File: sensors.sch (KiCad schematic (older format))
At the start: 18 parts

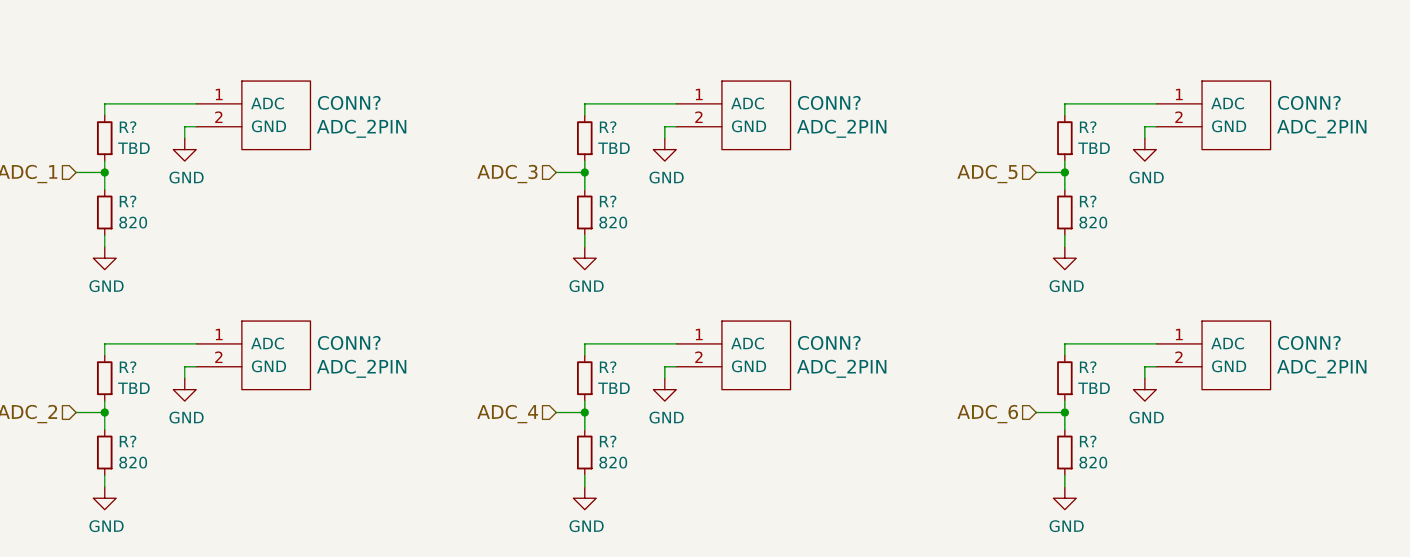
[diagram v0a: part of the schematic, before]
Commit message: Use 3pin connectors for ADC (with power pin)
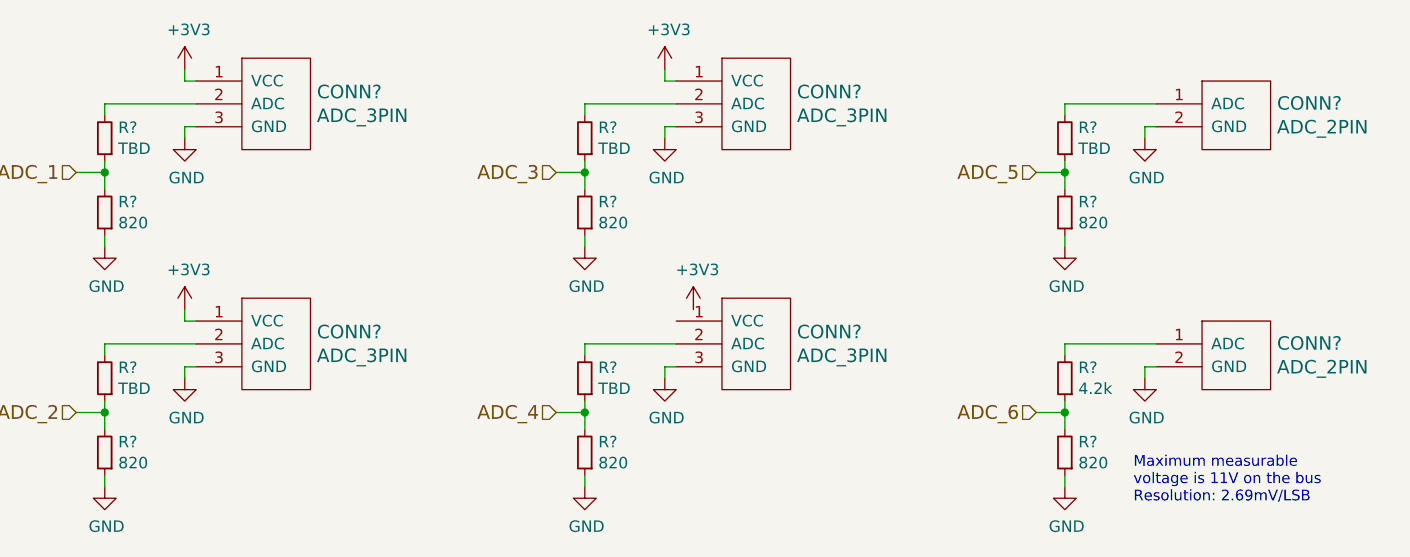
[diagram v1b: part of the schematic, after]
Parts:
- removed CONN? (x4): ADC_2PIN, symbol ADC_2PIN
- added CONN? (x4): ADC_3PIN, symbol ADC_3PIN
- R?: value TBD -> 4.2k
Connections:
- net GND: now also CONN?.3 (GND), CONN?.3 (GND), CONN?.3 (GND), CONN?.3 (GND)
- net at R?.2: now also CONN?.2 (ADC) (x4)
- new net +3V3: CONN?.1 (VCC), CONN?.1 (VCC), CONN?.1 (VCC)
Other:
- note added: "Maximum measurable \nvoltage is 11V on the bus\nResolution: 2.69mV/LSB"
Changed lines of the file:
@@
 Comment4 ""
 $EndDescr
-$Comp
-L ADC_2PIN CONN?
-U 1 1 569FF9E7
-P 2650 1750
-F 0 "CONN?" H 2828 2152 59  0000 L CNN
-F 1 "ADC_2PIN" H 2828 2048 59  0000 L CNN
-F 2 "" H 2650 1750 59  0000 C CNN
-F 3 "" H 2650 1750 59  0000 C CNN
-	1    2650 1750
-	1    0    0    -1
-$EndComp
 Text HLabel 1775 1650 0    60   Input ~ 0
 ADC_1
@@
 Wire Wire Line
 	1900 1975 1900 1925
-$Comp
-L ADC_2PIN CONN?
-U 1 1 56A00037
-P 2650 2800
-F 0 "CONN?" H 2828 3202 59  0000 L CNN
-F 1 "ADC_2PIN" H 2828 3098 59  0000 L CNN
-F 2 "" H 2650 2800 59  0000 C CNN
-F 3 "" H 2650 2800 59  0000 C CNN
-	1    2650 2800
-	1    0    0    -1
-$EndComp
 Text HLabel 1775 2700 0    60   Input ~ 0
 ADC_2
@@
 Wire Wire Line
 	1900 3025 1900 2975
-$Comp
-L ADC_2PIN CONN?
-U 1 1 56A00539
-P 4750 1750
-F 0 "CONN?" H 4928 2152 59  0000 L CNN
-F 1 "ADC_2PIN" H 4928 2048 59  0000 L CNN
-F 2 "" H 4750 1750 59  0000 C CNN
-F 3 "" H 4750 1750 59  0000 C CNN
-	1    4750 1750
-	1    0    0    -1
-$EndComp
 Text HLabel 3875 1650 0    60   Input ~ 0
 ADC_3
@@
 Wire Wire Line
 	4000 1975 4000 1925
-$Comp
-L ADC_2PIN CONN?
-U 1 1 56A00560
-P 4750 2800
-F 0 "CONN?" H 4928 3202 59  0000 L CNN
-F 1 "ADC_2PIN" H 4928 3098 59  0000 L CNN
-F 2 "" H 4750 2800 59  0000 C CNN
-F 3 "" H 4750 2800 59  0000 C CNN
-	1    4750 2800
-	1    0    0    -1
-$EndComp
 Text HLabel 3875 2700 0    60   Input ~ 0
 ADC_4
@@
 P 6100 2550
 F 0 "R?" H 6041 2504 50  0000 R CNN
-F 1 "TBD" H 6041 2596 50  0000 R CNN
+F 1 "4.2k" H 6041 2596 50  0000 R CNN
 F 2 "" H 6100 2550 50  0000 C CNN
 F 3 "" H 6100 2550 50  0000 C CNN
@@
 Wire Wire Line
 	6100 3025 6100 2975
+Text Notes 6400 3100 0    47   ~ 0
+Maximum measurable \nvoltage is 11V on the bus\nResolution: 2.69mV/LSB
+$Comp
+L ADC_3PIN CONN?
+U 1 1 56B05B1E
+P 2650 2800
+F 0 "CONN?" H 2828 3252 59  0000 L CNN
+F 1 "ADC_3PIN" H 2828 3148 59  0000 L CNN
+F 2 "" H 2650 2800 59  0000 C CNN
+F 3 "" H 2650 2800 59  0000 C CNN
+	1    2650 2800
+	1    0    0    -1
+$EndComp
+$Comp
+L ADC_3PIN CONN?
+U 1 1 56B05BE3
+P 2650 1750
+F 0 "CONN?" H 2828 2202 59  0000 L CNN
+F 1 "ADC_3PIN" H 2828 2098 59  0000 L CNN
+F 2 "" H 2650 1750 59  0000 C CNN
+F 3 "" H 2650 1750 59  0000 C CNN
+	1    2650 1750
+	1    0    0    -1
+$EndComp
+$Comp
+L +3V3 #PWR?
+U 1 1 56B05C70
+P 2250 2250
+F 0 "#PWR?" H 2250 2100 50  0001 C CNN
+F 1 "+3V3" H 2268 2424 50  0000 C CNN
+F 2 "" H 2250 2250 50  0000 C CNN
+F 3 "" H 2250 2250 50  0000 C CNN
+	1    2250 2250
+	1    0    0    -1
+$EndComp
+Wire Wire Line
+	2250 2250 2250 2300
+Wire Wire Line
+	2250 2300 2300 2300
+$Comp
+L +3V3 #PWR?
+U 1 1 56B05CFC
+P 2250 1200
+F 0 "#PWR?" H 2250 1050 50  0001 C CNN
+F 1 "+3V3" H 2268 1374 50  0000 C CNN
+F 2 "" H 2250 1200 50  0000 C CNN
+F 3 "" H 2250 1200 50  0000 C CNN
+	1    2250 1200
+	1    0    0    -1
+$EndComp
+Wire Wire Line
+	2250 1200 2250 1250
+Wire Wire Line
+	2250 1250 2300 1250
+$Comp
+L +3V3 #PWR?
+U 1 1 56B05E15
+P 4350 1200
+F 0 "#PWR?" H 4350 1050 50  0001 C CNN
+F 1 "+3V3" H 4368 1374 50  0000 C CNN
+F 2 "" H 4350 1200 50  0000 C CNN
+F 3 "" H 4350 1200 50  0000 C CNN
+	1    4350 1200
+	1    0    0    -1
+$EndComp
+$Comp
+L ADC_3PIN CONN?
+U 1 1 56B05E8E
+P 4750 1750
+F 0 "CONN?" H 4928 2202 59  0000 L CNN
+F 1 "ADC_3PIN" H 4928 2098 59  0000 L CNN
+F 2 "" H 4750 1750 59  0000 C CNN
+F 3 "" H 4750 1750 59  0000 C CNN
+	1    4750 1750
+	1    0    0    -1
+$EndComp
+Wire Wire Line
+	4350 1200 4350 1250
+Wire Wire Line
+	4350 1250 4400 1250
+$Comp
+L +3V3 #PWR?
+U 1 1 56B05F80
+P 4475 2250
+F 0 "#PWR?" H 4475 2100 50  0001 C CNN
+F 1 "+3V3" H 4493 2424 50  0000 C CNN
+F 2 "" H 4475 2250 50  0000 C CNN
+F 3 "" H 4475 2250 50  0000 C CNN
+	1    4475 2250
+	1    0    0    -1
+$EndComp
+$Comp
+L ADC_3PIN CONN?
+U 1 1 56B05FD2
+P 4750 2800
+F 0 "CONN?" H 4928 3252 59  0000 L CNN
+F 1 "ADC_3PIN" H 4928 3148 59  0000 L CNN
+F 2 "" H 4750 2800 59  0000 C CNN
+F 3 "" H 4750 2800 59  0000 C CNN
+	1    4750 2800
+	1    0    0    -1
+$EndComp
 $EndSCHEMATC

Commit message: Add RTC
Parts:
- added BT?: 3.6V, symbol Battery
- added C? (x2): 10p, symbol C_Small
- added C?: 220n, symbol C_Small
- added C?: 1u, symbol C_Small
- added U?: BQ32000, symbol BQ32000
- added X?: 32768Hz, symbol XTAL-SMD-4-PADS
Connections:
- net +3V3: now also C?.1, U?.8 (VCC)
- net GND: now also BT?.2, C?.2, C?.2, C?.2, C?.2, U?.4 (GND), X?.2 (case), X?.4 (case)
- new net: C?.1, U?.1 (OSCI), X?.3
- new net: C?.1, U?.2 (OSCO), X?.1
- new net: BT?.1, C?.1, U?.3 (V_BACK)
- new net I2C_SCL: U?.6 (SCL)
- new net I2C_SDA: U?.5 (SDA)
- no-connect marks 0 -> 1
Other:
- note added: "RTC\nI2C address: 0x68\nBattery: 1.4 to 3.6V"
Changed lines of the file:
@@
 Comment4 ""
 $EndDescr
-Text HLabel 1775 1650 0    60   Input ~ 0
+Text HLabel 1775 1650 0    47   Input ~ 0
 ADC_1
 $Comp
@@
 	1900 1350 2300 1350
 Wire Wire Line
-	1900 1600 1900 1725
+	1900 1600 1900 1650
+Wire Wire Line
+	1900 1650 1900 1725
 Wire Wire Line
 	1775 1650 1900 1650
@@
 Wire Wire Line
 	1900 1975 1900 1925
-Text HLabel 1775 2700 0    60   Input ~ 0
+Text HLabel 1775 2700 0    47   Input ~ 0
 ADC_2
 $Comp
@@
 	1900 2400 2300 2400
 Wire Wire Line
-	1900 2650 1900 2775
+	1900 2650 1900 2700
+Wire Wire Line
+	1900 2700 1900 2775
 Wire Wire Line
 	1775 2700 1900 2700
@@
 Wire Wire Line
 	1900 3025 1900 2975
-Text HLabel 3875 1650 0    60   Input ~ 0
+Text HLabel 3875 1650 0    47   Input ~ 0
 ADC_3
 $Comp
@@
 	4000 1350 4400 1350
 Wire Wire Line
-	4000 1600 4000 1725
+	4000 1600 4000 1650
+Wire Wire Line
+	4000 1650 4000 1725
 Wire Wire Line
 	3875 1650 4000 1650
@@
 Wire Wire Line
 	4000 1975 4000 1925
-Text HLabel 3875 2700 0    60   Input ~ 0
+Text HLabel 3875 2700 0    47   Input ~ 0
 ADC_4
 $Comp
@@
 	4000 2400 4400 2400
 Wire Wire Line
-	4000 2650 4000 2775
+	4000 2650 4000 2700
+Wire Wire Line
+	4000 2700 4000 2775
 Wire Wire Line
 	3875 2700 4000 2700
@@
 	1    0    0    -1
 $EndComp
-Text HLabel 5975 1650 0    60   Input ~ 0
+Text HLabel 5975 1650 0    47   Input ~ 0
 ADC_5
 $Comp
@@
 	6100 1350 6500 1350
 Wire Wire Line
-	6100 1600 6100 1725
+	6100 1600 6100 1650
+Wire Wire Line
+	6100 1650 6100 1725
 Wire Wire Line
 	5975 1650 6100 1650
@@
 	1    0    0    -1
 $EndComp
-Text HLabel 5975 2700 0    60   Input ~ 0
+Text HLabel 5975 2700 0    47   Input ~ 0
 ADC_6
 $Comp
@@
 	6100 2400 6500 2400
 Wire Wire Line
-	6100 2650 6100 2775
+	6100 2650 6100 2700
+Wire Wire Line
+	6100 2700 6100 2775
 Wire Wire Line
 	5975 2700 6100 2700
@@
 	1    0    0    -1
 $EndComp
+$Comp
+L BQ32000 U?
+U 1 1 56B4E3C0
+P 3500 5025
+F 0 "U?" H 3500 5609 59  0000 C CNN
+F 1 "BQ32000" H 3500 5505 59  0000 C CNN
+F 2 "" H 3500 5675 39  0000 C CNN
+F 3 "" H 3500 5675 39  0000 C CNN
+	1    3500 5025
+	1    0    0    -1
+$EndComp
+Text HLabel 4050 4725 2    47   Input ~ 0
+I2C_SCL
+Text HLabel 4050 4825 2    47   Input ~ 0
+I2C_SDA
+NoConn ~ 4050 5025
+Wire Wire Line
+	4050 5325 4800 5325
+Wire Wire Line
+	4150 5625 4100 5625
+Wire Wire Line
+	4100 5425 4100 5625
+Wire Wire Line
+	4100 5625 4100 5725
+Wire Wire Line
+	4100 5425 4050 5425
+$Comp
+L C_Small C?
+U 1 1 56B4F39B
+P 4100 5825
+F 0 "C?" H 4192 5863 39  0000 L CNN
+F 1 "10p" H 4192 5787 39  0000 L CNN
+F 2 "" H 4100 5825 50  0000 C CNN
+F 3 "" H 4100 5825 50  0000 C CNN
+	1    4100 5825
+	1    0    0    -1
+$EndComp
+$Comp
+L C_Small C?
+U 1 1 56B4F45D
+P 4800 5825
+F 0 "C?" H 4892 5863 39  0000 L CNN
+F 1 "10p" H 4892 5787 39  0000 L CNN
+F 2 "" H 4800 5825 50  0000 C CNN
+F 3 "" H 4800 5825 50  0000 C CNN
+	1    4800 5825
+	1    0    0    -1
+$EndComp
+Connection ~ 4100 5625
+$Comp
+L GND #PWR?
+U 1 1 56B4F5FE
+P 4450 6025
+F 0 "#PWR?" H 4450 5775 50  0001 C CNN
+F 1 "GND" H 4458 5851 50  0000 C CNN
+F 2 "" H 4450 6025 50  0000 C CNN
+F 3 "" H 4450 6025 50  0000 C CNN
+	1    4450 6025
+	1    0    0    -1
+$EndComp
+$Comp
+L XTAL-SMD-4-PADS X?
+U 1 1 56B4F654
+P 4450 5625
+F 0 "X?" H 4625 5675 47  0000 C CNN
+F 1 "32768Hz" H 4450 5775 47  0000 C CNN
+F 2 "" H 4450 5625 60  0000 C CNN
+F 3 "" H 4450 5625 60  0000 C CNN
+	1    4450 5625
+	1    0    0    -1
+$EndComp
+Wire Wire Line
+	4800 5325 4800 5625
+Wire Wire Line
+	4800 5625 4800 5725
+Wire Wire Line
+	4800 5625 4750 5625
+Connection ~ 4800 5625
+Wire Wire Line
+	4450 5975 4450 6025
+Wire Wire Line
+	4100 5975 4400 5975
+Wire Wire Line
+	4400 5975 4450 5975
+Wire Wire Line
+	4450 5975 4500 5975
+Wire Wire Line
+	4500 5975 4800 5975
+Wire Wire Line
+	4100 5975 4100 5925
+Wire Wire Line
+	4800 5975 4800 5925
+Connection ~ 4450 5975
+Wire Wire Line
+	4500 5975 4500 5825
+Connection ~ 4500 5975
+Wire Wire Line
+	4400 5825 4400 5975
+Connection ~ 4400 5975
+$Comp
+L C_Small C?
+U 1 1 56B4FEC7
+P 2850 5225
+F 0 "C?" H 2942 5271 50  0000 L CNN
+F 1 "220n" H 2942 5179 50  0000 L CNN
+F 2 "" H 2850 5225 50  0000 C CNN
+F 3 "" H 2850 5225 50  0000 C CNN
+	1    2850 5225
+	1    0    0    -1
+$EndComp
+$Comp
+L GND #PWR?
+U 1 1 56B4FF6E
+P 2175 5475
+F 0 "#PWR?" H 2175 5225 50  0001 C CNN
+F 1 "GND" H 2183 5301 50  0000 C CNN
+F 2 "" H 2175 5475 50  0000 C CNN
+F 3 "" H 2175 5475 50  0000 C CNN
+	1    2175 5475
+	1    0    0    -1
+$EndComp
+$Comp
+L C_Small C?
+U 1 1 56B4FFB0
+P 2175 5025
+F 0 "C?" H 2267 5071 50  0000 L CNN
+F 1 "1u" H 2267 4979 50  0000 L CNN
+F 2 "" H 2175 5025 50  0000 C CNN
+F 3 "" H 2175 5025 50  0000 C CNN
+	1    2175 5025
+	1    0    0    -1
+$EndComp
+$Comp
+L +3V3 #PWR?
+U 1 1 56B500CE
+P 2175 4675
+F 0 "#PWR?" H 2175 4525 50  0001 C CNN
+F 1 "+3V3" H 2193 4849 50  0000 C CNN
+F 2 "" H 2175 4675 50  0000 C CNN
+F 3 "" H 2175 4675 50  0000 C CNN
+	1    2175 4675
+	1    0    0    -1
+$EndComp
+Wire Wire Line
+	2175 5125 2175 5425
+Wire Wire Line
+	2175 5425 2175 5475
+Wire Wire Line
+	2175 4675 2175 4725
+Wire Wire Line
+	2175 4725 2175 4925
+Wire Wire Line
+	2950 4725 2175 4725
+Connection ~ 2175 4725
+Wire Wire Line
+	2175 5425 2500 5425
+Wire Wire Line
+	2500 5425 2850 5425
+Wire Wire Line
+	2850 5425 2950 5425
+Connection ~ 2175 5425
+Wire Wire Line
+	2850 5325 2850 5425
+Connection ~ 2850 5425
+Wire Wire Line
+	2500 5025 2850 5025
+Wire Wire Line
+	2850 5025 2950 5025
+Wire Wire Line
+	2850 5025 2850 5125
+$Comp
+L Battery BT?
+U 1 1 56B503FF
+P 2500 5225
+F 0 "BT?" H 2618 5263 39  0000 L CNN
+F 1 "3.6V" H 2618 5187 39  0000 L CNN
+F 2 "" V 2500 5265 50  0000 C CNN
+F 3 "" V 2500 5265 50  0000 C CNN
+	1    2500 5225
+	1    0    0    -1
+$EndComp
+Wire Wire Line
+	2500 5375 2500 5425
+Connection ~ 2500 5425
+Wire Wire Line
+	2500 5075 2500 5025
+Connection ~ 2850 5025
+Text Notes 4000 4425 0    47   ~ 0
+RTC\nI2C address: 0x68\nBattery: 1.4 to 3.6V
 $EndSCHEMATC

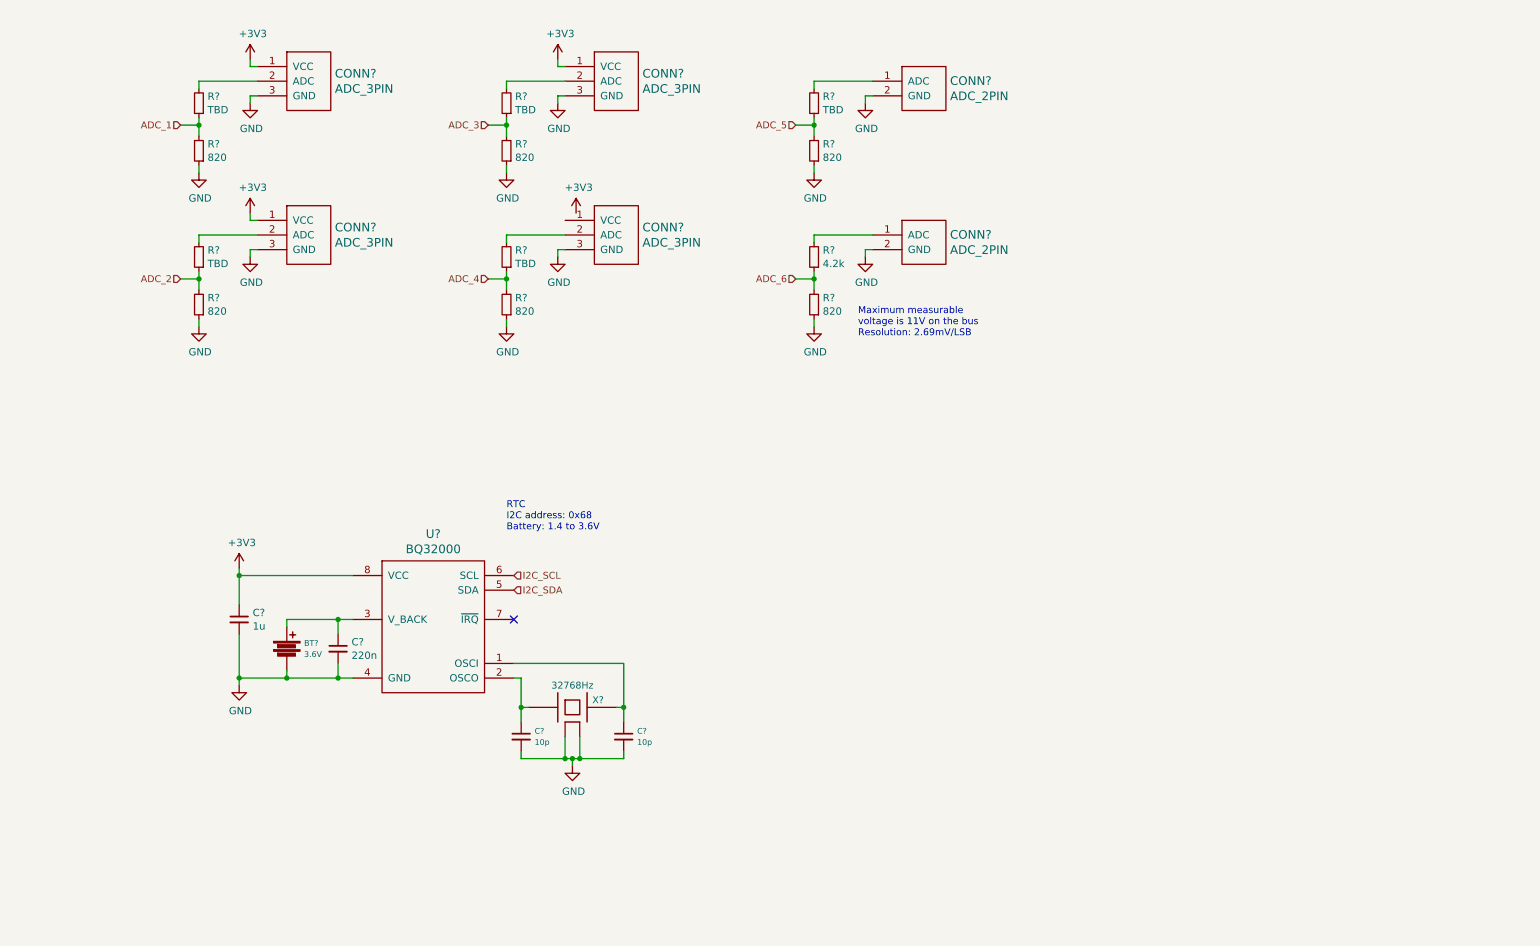
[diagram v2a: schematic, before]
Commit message: Add digital inputs with power option
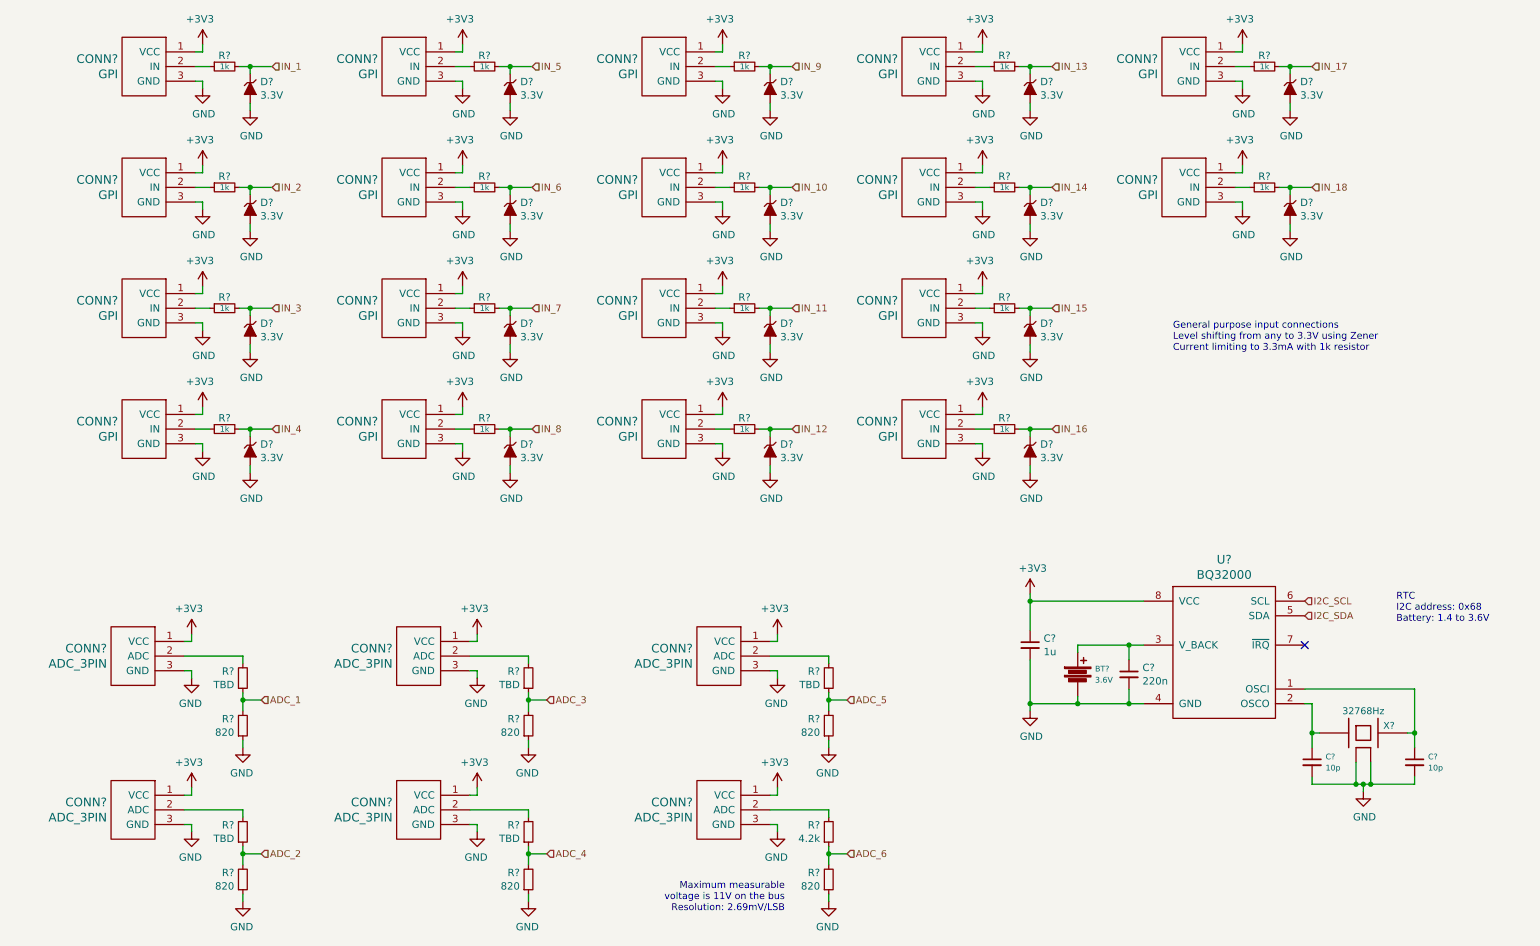
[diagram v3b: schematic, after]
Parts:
- removed CONN? (x2): ADC_2PIN, symbol ADC_2PIN
- added CONN? (x18): GPI, symbol GPI
- added CONN? (x2): ADC_3PIN, symbol ADC_3PIN
- added D? (x18): 3.3V, symbol ZENERsmall
- added R? (x18): 1k, symbol R_Small
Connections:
- net +3V3: now also CONN?.1 (VCC), CONN?.1 (VCC), CONN?.1 (VCC), CONN?.1 (VCC), CONN?.1 (VCC), CONN?.1 (VCC), CONN?.1 (VCC), CONN?.1 (VCC), CONN?.1 (VCC), CONN?.1 (VCC), CONN?.1 (VCC), CONN?.1 (VCC), CONN?.1 (VCC), CONN?.1 (VCC), CONN?.1 (VCC), CONN?.1 (VCC), CONN?.1 (VCC), CONN?.1 (VCC), CONN?.1 (VCC), CONN?.1 (VCC), CONN?.1 (VCC)
- net GND: now also CONN?.3 (GND), CONN?.3 (GND), CONN?.3 (GND), CONN?.3 (GND), CONN?.3 (GND), CONN?.3 (GND), CONN?.3 (GND), CONN?.3 (GND), CONN?.3 (GND), CONN?.3 (GND), CONN?.3 (GND), CONN?.3 (GND), CONN?.3 (GND), CONN?.3 (GND), CONN?.3 (GND), CONN?.3 (GND), CONN?.3 (GND), CONN?.3 (GND), CONN?.3 (GND), CONN?.3 (GND), D?.2 (A), D?.2 (A), D?.2 (A), D?.2 (A), D?.2 (A), D?.2 (A), D?.2 (A), D?.2 (A), D?.2 (A), D?.2 (A), D?.2 (A), D?.2 (A), D?.2 (A), D?.2 (A), D?.2 (A), D?.2 (A), D?.2 (A), D?.2 (A)
- net at R?.2: now also CONN?.2 (ADC) (x2)
- new net: CONN?.2 (IN), R?.1 (x18)
- new net IN_1: D?.1 (K), R?.2
- new net IN_10: D?.1 (K), R?.2
- new net IN_11: D?.1 (K), R?.2
- new net IN_12: D?.1 (K), R?.2
- new net IN_13: D?.1 (K), R?.2
- new net IN_14: D?.1 (K), R?.2
- new net IN_15: D?.1 (K), R?.2
- new net IN_16: D?.1 (K), R?.2
- new net IN_17: D?.1 (K), R?.2
- new net IN_18: D?.1 (K), R?.2
- new net IN_2: D?.1 (K), R?.2
- new net IN_3: D?.1 (K), R?.2
- new net IN_4: D?.1 (K), R?.2
- new net IN_5: D?.1 (K), R?.2
- new net IN_6: D?.1 (K), R?.2
- new net IN_7: D?.1 (K), R?.2
- new net IN_8: D?.1 (K), R?.2
- new net IN_9: D?.1 (K), R?.2
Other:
- note added: "General purpose input connections\nLevel shifting from any to 3.3V using Zener\nCurrent limiting to 3.3mA with 1k resistor"
- moved on the sheet: BT?, C?, CONN?, R?, U?, X?

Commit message: Annotate
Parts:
- gave numbers to parts that had none: 79
